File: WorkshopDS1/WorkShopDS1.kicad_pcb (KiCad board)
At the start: 2 copper layers, 21 parts

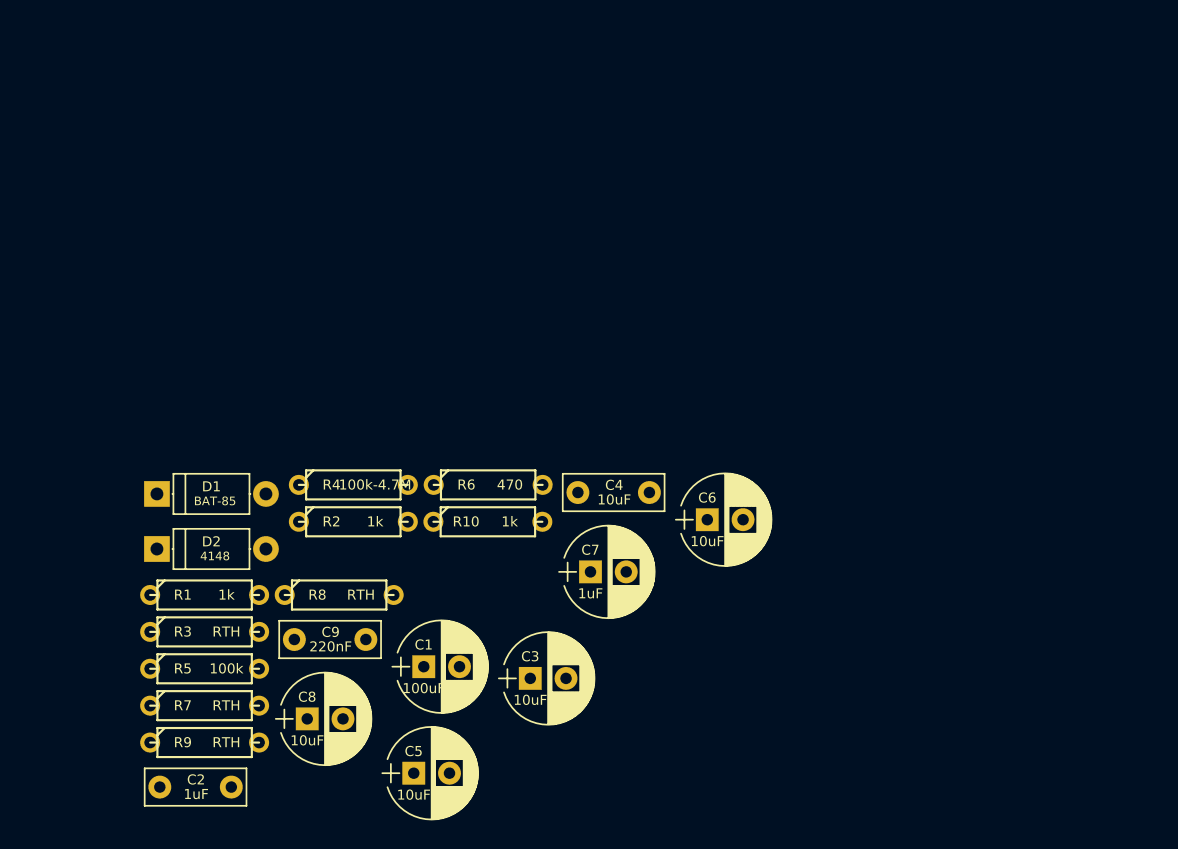
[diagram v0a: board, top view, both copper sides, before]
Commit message: got rid of extra parts - changed a few footprints
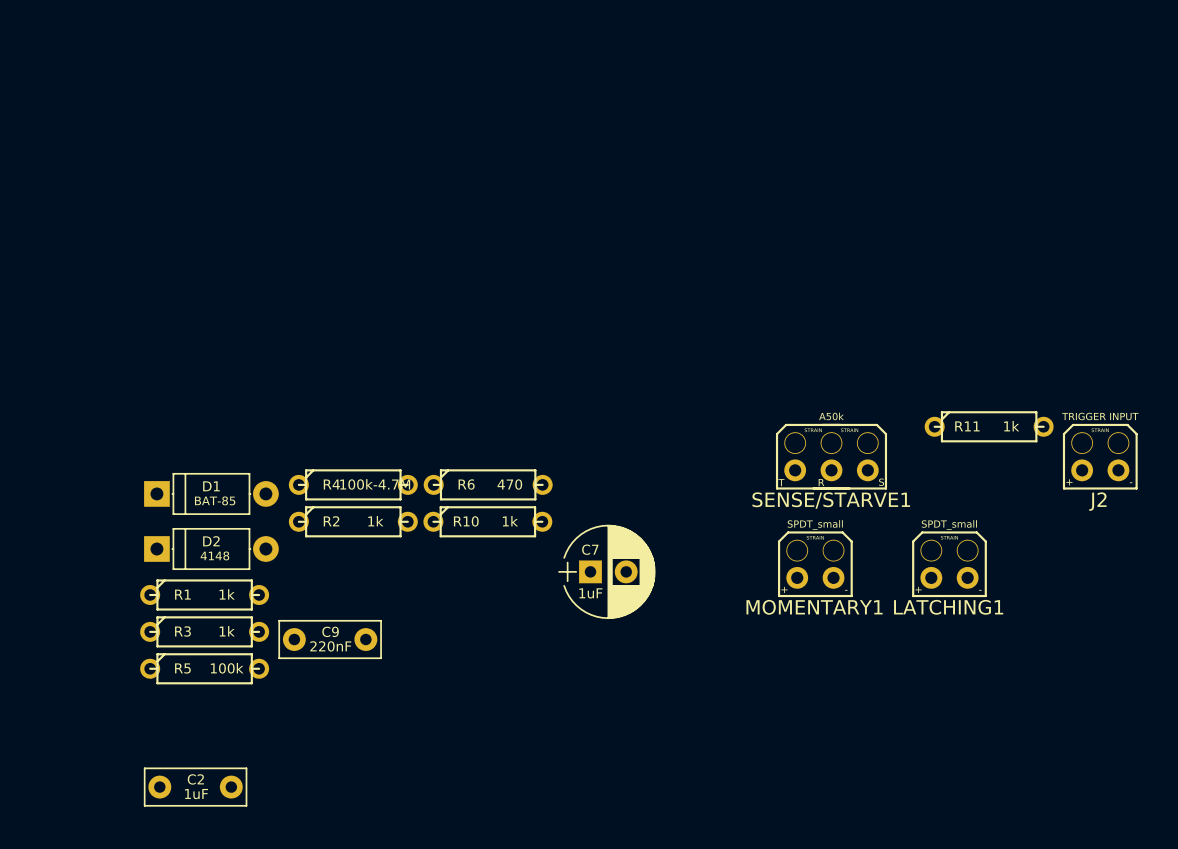
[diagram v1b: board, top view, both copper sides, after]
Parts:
- removed C1: 100uF, 4ms-footprints:Cap_Electrolytic_TH
- removed C3, C5, C6, C8: 10uF, 4ms-footprints:Cap_Electrolytic_TH
- removed C4: 10uF, 4ms-footprints:Cap_Ceramic_TH
- removed R7, R8, R9: RTH, 4ms-footprints:Resistor_TH_300
- added J2: TRIGGER INPUT, zfoot:Jack_DC, F.Cu at (180.1, 57.8)
- added LATCHING1: SPDT_small, zfoot:Jack_DC, F.Cu at (169.5, 65.3)
- added MOMENTARY1: SPDT_small, zfoot:Jack_DC, F.Cu at (160.1, 65.3)
- added R11: 1k, 4ms-footprints:Resistor_TH_300, F.Cu at (172.3, 54.8)
- added SENSE/STARVE1: A50k, zfoot:Jack_Instrument_exp, F.Cu at (161.3, 57.8)
- R3: value RTH -> 1k
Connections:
- D1 pad 1: Net-(C1-Pad1) -> +9V

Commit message: forgot to save
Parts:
- added J1: 9v battery, zfoot:Jack_DC, F.Cu at (127.9, 38.8)
- added J3: OUTPUT, zfoot:Jack_Instrument, F.Cu at (117.6, 45.7)
- added LED2: LED, zfoot:Jack_DC, F.Cu at (136.1, 31.3)
- added PITCH1: B50k, zfoot:Jack_Instrument_exp, F.Cu at (129.2, 31.3)
- added U1: 7414, 4ms-footprints:DIP-14_W7.62mm, F.Cu at (105.9, 30.3)
- added U2: LM358, 4ms-footprints:DIP_8pin_TL072_TH, F.Cu at (116.2, 30.3)
